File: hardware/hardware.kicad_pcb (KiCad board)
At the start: 2 copper layers, 14.6 x 8 mm, 25 parts, among them J1 USB_B_Micro, J2 Conn_Coaxial, Q1 BSS138, Q2 BSS138, U1 ESP32-WROOM-32, U2 AMS1117-3.3, U4 CH340C, U5 RFM95W-868S2

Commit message: lora wiring + pcb wiring
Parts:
- added J3: Conn_01x04, Connector_PinHeader_2.54mm:PinHeader_1x04_P2.54mm_Vertical, F.Cu at (112.5, 90.0)
- moved R4 30.0 mm to (92.2, 61.4), turned to -90 degrees
- moved C5 27.4 mm to (94.0, 96.7), turned to -90 degrees
- moved BOOT1 26.3 mm to (85.3, 61.9), turned to 180 degrees
- moved C1 20.2 mm to (101.5, 90.9), turned to 180 degrees
- moved C6 19.4 mm to (115.4, 69.9), turned to -90 degrees
- moved J2 15.6 mm to (117.3, 77.2)
- moved U2 10.0 mm to (101.6, 85.6)
- moved U5 9.47 mm to (105.1, 70.1)
- moved C3 7.60 mm to (107.8, 84.2)
- moved EN1 6.82 mm to (94.9, 84.3), turned to -90 degrees
- moved C2 5.37 mm to (109.5, 84.2), turned to -90 degrees
- moved Q1 4.36 mm to (91.0, 97.0)
- moved Q2 4.16 mm to (91.0, 92.5)
- moved D2 2.38 mm to (74.0, 88.0), turned to 0 degrees
- moved U4 1.00 mm to (82.5, 91.0)
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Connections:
- R5 pad 1: Net-(U1-IO12) -> Net-(U1-IO26)
- R6 pad 1: Net-(U1-IO13) -> Net-(U1-IO27)
- U1 pad 11: unconnected-(U1-IO26-Pad11) -> Net-(U1-IO26)
- U1 pad 12: unconnected-(U1-IO27-Pad12) -> Net-(U1-IO27)
- U1 pad 13: unconnected-(U1-IO14-Pad13) -> SCLK
- U1 pad 14: Net-(U1-IO12) -> MISO
- U1 pad 16: Net-(U1-IO13) -> MOSI
- U1 pad 23: unconnected-(U1-IO15-Pad23) -> SS
- U1 pad 27: unconnected-(U1-IO16-Pad27) -> DIO0
- U1 pad 28: unconnected-(U1-IO17-Pad28) -> DIO1
- U1 pad 30: unconnected-(U1-IO18-Pad30) -> DIO2
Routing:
- net +3V3: track 0.00 -> 126.8 mm, vias 0 -> 4
- net SCL: track 0.00 -> 73.0 mm
- net SDA: track 0.00 -> 71.6 mm
- net ESP32_IO0: track 0.00 -> 39.0 mm, vias 0 -> 2
- net ESP32_EN: track 0.00 -> 36.5 mm, vias 0 -> 4
- net +5V: track 0.00 -> 33.4 mm, vias 0 -> 2
- net DIO2: track 0.00 -> 32.5 mm, vias 0 -> 2
- net DIO1: track 0.00 -> 30.2 mm, vias 0 -> 2
- net RX-PROG: track 0.00 -> 29.1 mm, vias 0 -> 2
- net TX-PROG: track 0.00 -> 28.9 mm, vias 0 -> 2
- net DIO0: track 0.00 -> 28.3 mm, vias 0 -> 2
- net Net-(Q1-S): track 0.00 -> 26.2 mm
- net SCLK: track 0.00 -> 23.3 mm, vias 0 -> 2
- net MISO: track 0.00 -> 23.2 mm, vias 0 -> 2
- net MOSI: track 0.00 -> 16.2 mm
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- added copper zone on B.Cu, net GND
- added copper zone on F.Cu, net GND
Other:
- board size 14.6 x 8 mm -> 47.5 x 42 mm

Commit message: invert i2c screen wiring
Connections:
- J3 pad 1: SCL -> SDA
- J3 pad 2: SDA -> SCL
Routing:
- net SDA: track 71.6 -> 73.4 mm
- net GND: vias 25 -> 36

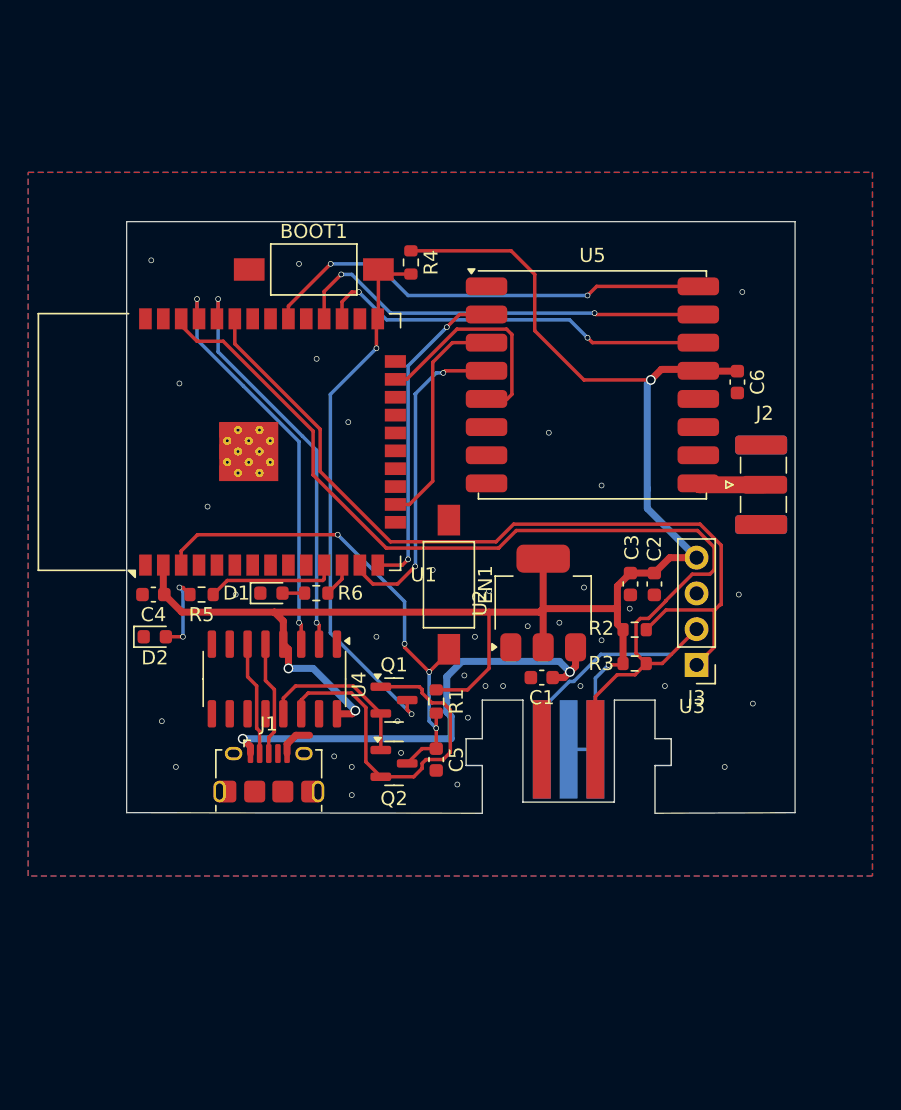
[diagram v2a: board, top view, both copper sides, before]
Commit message: add second nunchuck connector and pcb wiring
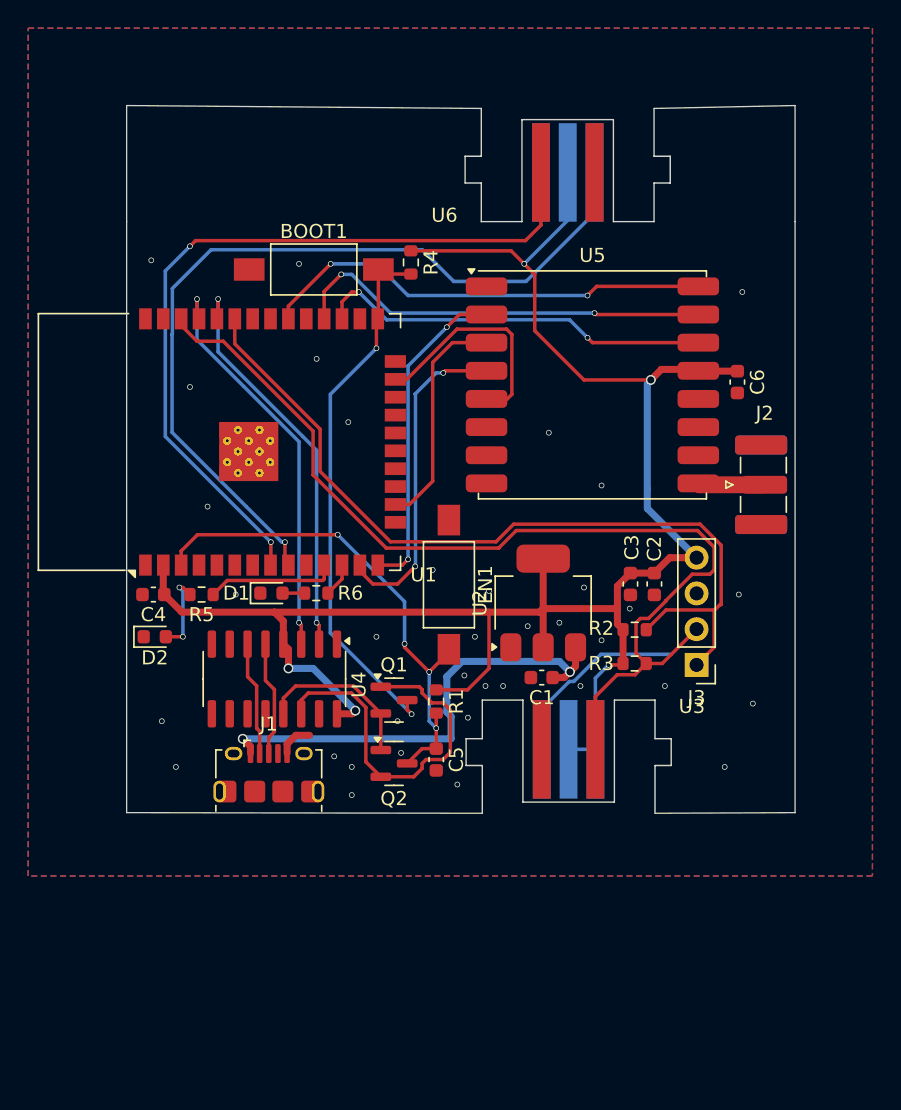
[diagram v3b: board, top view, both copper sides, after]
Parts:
- added U6: ~, nunchcuk:nunchuck, F.Cu at (101.4, 55.0)
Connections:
- U1 pad 8: unconnected-(U1-IO32-Pad8) -> SCL2
- U1 pad 9: unconnected-(U1-IO33-Pad9) -> SDA2
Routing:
- net SDA2: track 0.00 -> 65.7 mm, vias 0 -> 1
- net SCL2: track 0.00 -> 55.8 mm, vias 0 -> 2
- net +3V3: track 126.8 -> 134.6 mm, vias 4 -> 5
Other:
- board size 47.5 x 42 mm -> 47.5 x 50.3 mm

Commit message: add ftdi pin and wiring to esp
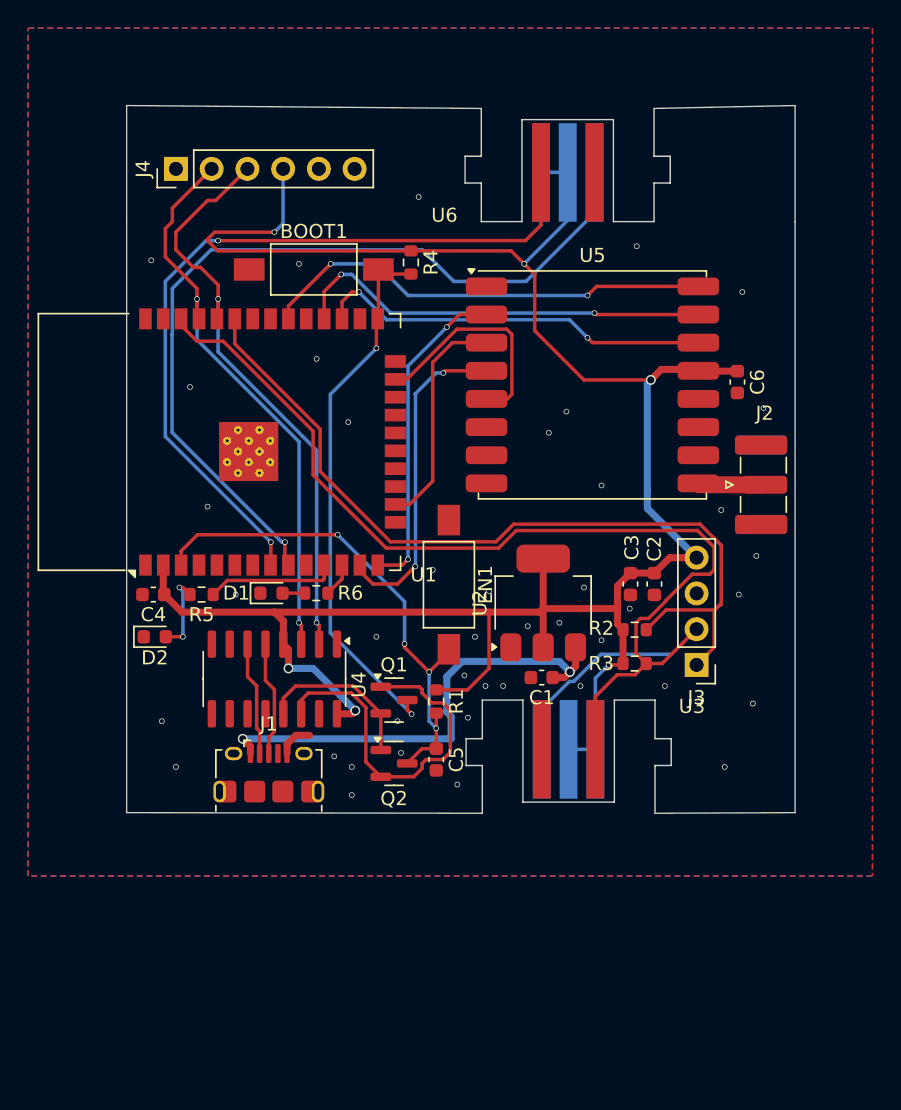
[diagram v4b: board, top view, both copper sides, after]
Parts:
- added J4: Conn_01x06, Connector_PinHeader_2.54mm:PinHeader_1x06_P2.54mm_Vertical, F.Cu at (75.5, 54.8)
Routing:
- net +3V3: track 134.6 -> 161.0 mm, vias 5 -> 6
- net TX-PROG: track 28.9 -> 42.2 mm
- net RX-PROG: track 29.1 -> 40.6 mm
- net GND: vias 36 -> 42

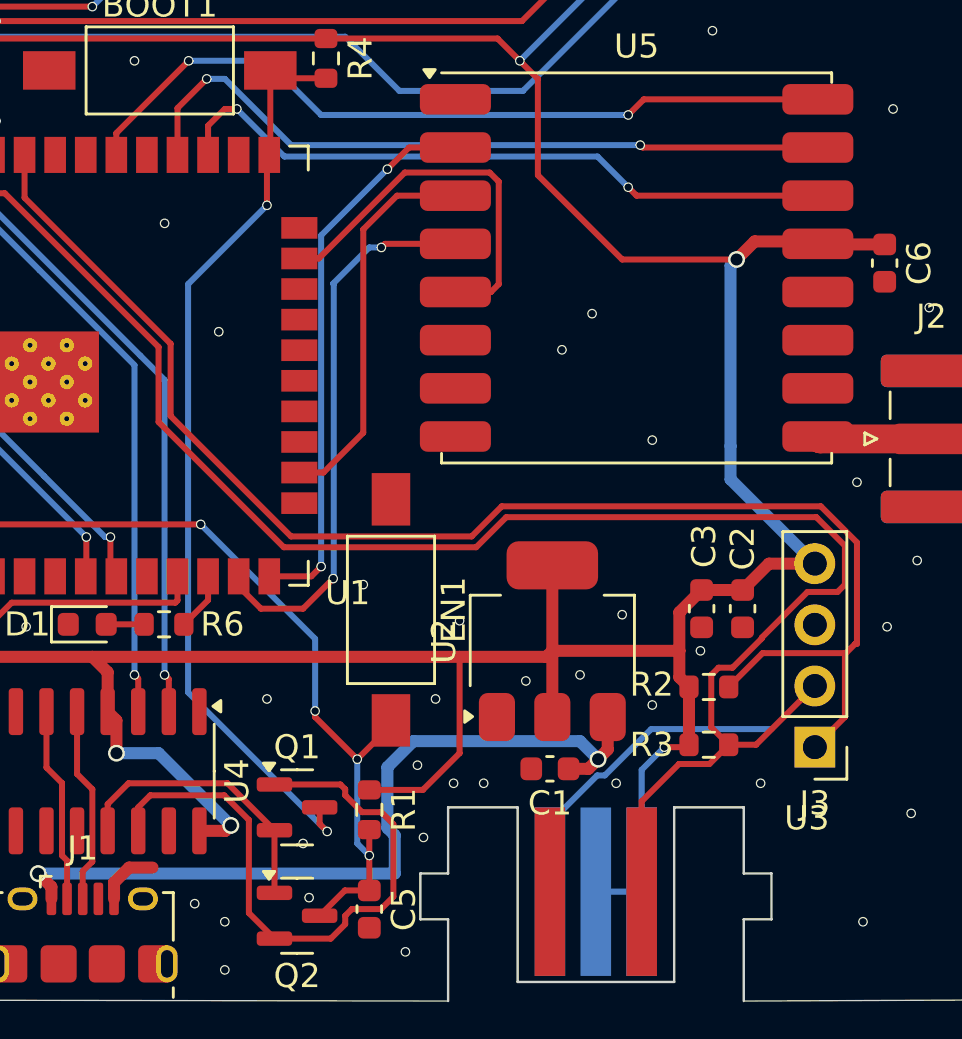
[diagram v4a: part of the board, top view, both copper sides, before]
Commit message: fix i2c wiring and lora rst
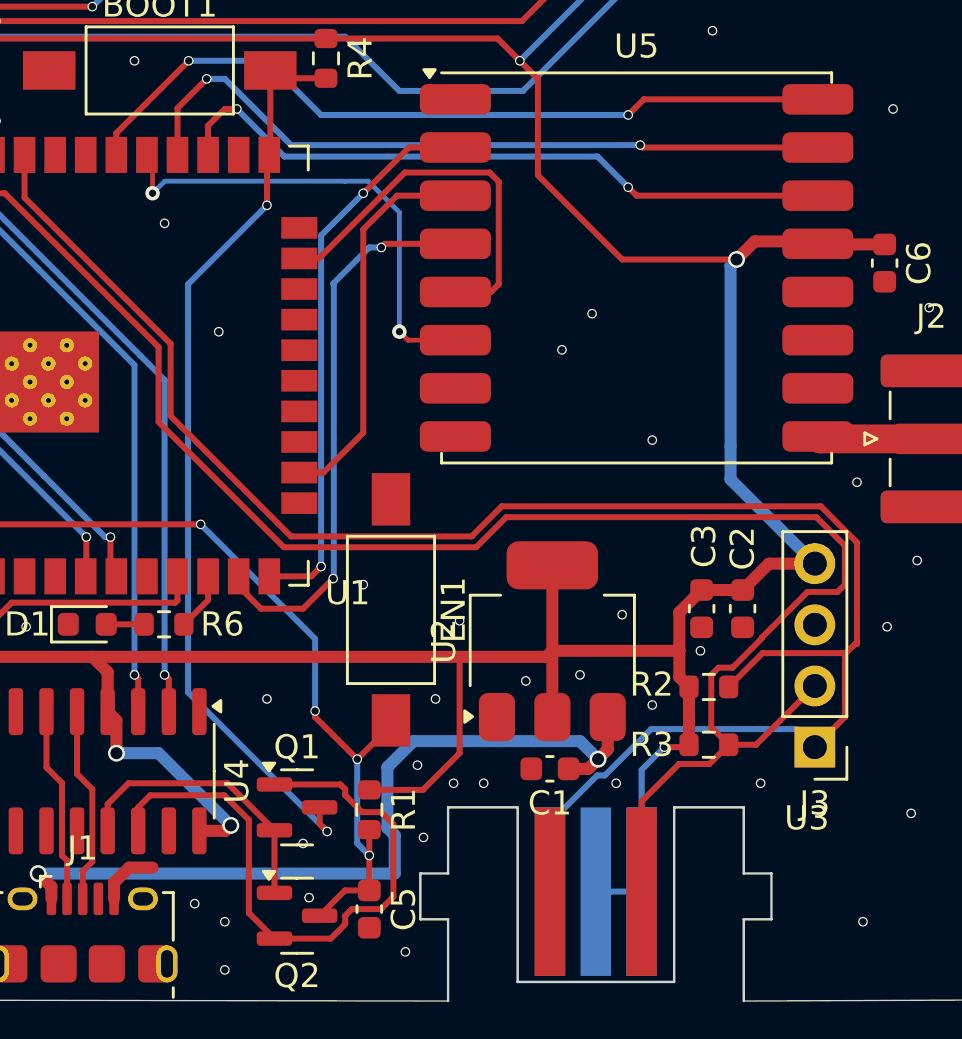
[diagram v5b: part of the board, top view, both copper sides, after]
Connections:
- U1 pad 29: unconnected-(U1-IO5-Pad29) -> LORA_RST
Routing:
- net LORA_RST: track 0.00 -> 20.1 mm, vias 0 -> 2
- net SDA: track 73.4 -> 75.5 mm
